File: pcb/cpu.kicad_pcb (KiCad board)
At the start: 2 copper layers, 270 parts, among them J1 Conn_01x05, J2 Conn_02x20_Odd_Even, J3 Conn_01x03, J4 Conn_02x20_Odd_Even, SW1 SW_DIP_x03 - Clock Source Sel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, SW2 SW_Push, SW4 SW_Push, U1 LM555, U10 74HCT574, U11 74LS283, U112 74LS574, U113 SST39SF040, U114 74HC04, U12 74HCT574, U121 74HCT574, U13 74LS273, U14 74LS283, U15 74LS273, U16 74HC245, U17 74HC238, U18 74HC245, U19 74HC238, U2 74HC14, U20 74HC238, U21 74HC00, U22 74LS283, U23 74LS283, U24 74HC245, U25 74HC245, U26 74HC00, U27 74LS283, U28 74LS283, U29 74HC245, U3 74151, U30 74HC86, U31 74HC245, U32 74HC00, U33 74LS08, U34 74LS283, U35 74LS107, U36 74HC238, U37 74LS138, U38 74LS574, U39 74HC590, U4 LM555 - Button Clock, U40 74LS283, U41 74HC245, U42 74HC245, U43 74HC00, U44 74HC00, U45 74HC00, U46 74HC00, U47 74HC00, U48 74HCT574, U49 74HCT574, U5 74HC04, U50 74HCT574, U51 74HCT574, U52 74HCT574, U53 74HCT574, U54 74HCT574, U55 74HCT574, U56 74HCT574, U57 74HCT574, U58 74HCT574, U59 74HCT574, U6 74HC590, U60 74HCT574, U61 74HCT574, U62 74HCT574, U63 74HCT574, U64 74HCT574, U65 74HCT574, U66 74LS32, U67 74HCT574, U68 74HCT574, U69 74HCT574, U7 74LS574, U70 74HCT574, U71 SST39SF040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

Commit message: About to try reducing by 1 EEPROM and reducing number of chips.
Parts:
- moved C103 394.5 mm to (211.5, 43.5)
- moved U86 394.5 mm to (215.0, 50.0)
- moved C17 331.6 mm to (155.5, 122.0)
- moved C18 331.6 mm to (159.0, 94.0)
- moved C19 331.6 mm to (159.0, 105.5)
- moved C23 331.6 mm to (155.5, 94.0)
- moved C26 331.6 mm to (171.0, 117.5)
- moved C34 331.6 mm to (171.0, 132.0)
- moved C60 331.6 mm to (133.5, 125.0)
- moved D1 331.6 mm to (167.0, 118.5)
- moved D2 331.6 mm to (167.0, 122.0)
- moved D3 331.6 mm to (167.0, 125.5)
- moved D4 331.6 mm to (167.0, 129.0)
- moved D5 331.6 mm to (167.0, 132.5)
- moved D6 331.6 mm to (167.0, 136.0)
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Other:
- board outline added: 235 x 190 mm
- net class CLK_NETS added: clearance 0.5, trace_width 0.2, via_dia 0.6, via_drill 0.3
- net class Default: clearance 0.14 -> 0.1; trace_width 0.2 -> 0.1
- net class POWER_NETS added: clearance 0.2, trace_width 0.3, via_dia 0.6, via_drill 0.3
- rule trace_clearance: 0.14 -> 0.1
- rule trace_min: 0.2 -> 0.1
- board text added: "Clk Sel Change Latch"
- board text added: "MemePU Ver.2.67 - MEME EDITION"
- board text removed: "Registers"

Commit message: Removed 1 EEPROM and some other chips by moving BUS_OUT signals to multi-plane.
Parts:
- removed C106, C107, C124, C125: 0.1uF, Capacitor_THT:C_Disc_D6.0mm_W2.5mm_P5.00mm
- removed U113: SST39SF040, Package_DIP:DIP-32_W15.24mm_Socket
- removed U114: 74HC04, Package_DIP:DIP-14_W7.62mm_Socket
- removed U95, U96: 74LS154, Package_DIP:DIP-24_W7.62mm_Socket
- added C104: 0.1uF, Capacitor_THT:C_Disc_D6.0mm_W2.5mm_P5.00mm, F.Cu at (104.5, 59.0)
- added U91: 74LS154, Package_DIP:DIP-24_W7.62mm_Socket, F.Cu at (101.0, 57.5)
- moved C103 199.3 mm to (13.0, 61.0)
- moved C94 199.3 mm to (13.0, 49.5)
- moved U85 199.3 mm to (16.5, 56.5)
- moved U86 199.3 mm to (16.5, 67.5)
- moved C22 101.1 mm to (216.5, 23.5), turned to 270 degrees
- moved U10 96.8 mm to (220.0, 30.0), turned to 90 degrees
- moved C21 83.5 mm to (186.5, 23.5), turned to 270 degrees
- moved U9 78.4 mm to (190.0, 30.5), turned to 90 degrees
- moved RN1 76.4 mm to (152.5, 37.0)
- moved C20 65.7 mm to (156.5, 23.0), turned to 270 degrees
- moved J4 60.5 mm to (191.0, 17.0)
- moved U8 60.0 mm to (160.0, 30.0), turned to 90 degrees
- moved J2 59.5 mm to (131.5, 17.0)
- moved U39 58.1 mm to (39.5, 12.5)
- moved U20 54.0 mm to (123.5, 12.5), turned to 270 degrees
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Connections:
- J2 pad 10: /BUS10 -> /BUS4
- J2 pad 12: /BUS11 -> /BUS5
- J2 pad 14: /BUS12 -> /BUS6
- J2 pad 16: /BUS13 -> /BUS7
- J2 pad 18: /BUS14 -> /BUS8
- J2 pad 2: /BUS6 -> /BUS0
- J2 pad 20: /BUS15 -> /BUS9
- J2 pad 22: /BUS16 -> /BUS10
- J2 pad 24: /BUS17 -> /BUS11
- J2 pad 26: /BUS18 -> /BUS12
- J2 pad 28: /BUS19 -> /BUS13
- J2 pad 29: /BUS0 -> /ADDR0
- J2 pad 30: /BUS20 -> /BUS14
- J2 pad 31: /BUS1 -> /ADDR1
- J2 pad 32: /BUS21 -> /BUS15
- J2 pad 33: /BUS2 -> /ADDR2
- J2 pad 34: /BUS22 -> /BUS16
- J2 pad 35: /BUS3 -> /ADDR3
- J2 pad 36: /BUS23 -> /BUS17
- J2 pad 37: /BUS4 -> /ADDR4
- J2 pad 38: /BUS24 -> /BUS18
- J2 pad 39: /BUS5 -> /ADDR5
- J2 pad 4: /BUS7 -> /BUS1
- J2 pad 40: /BUS25 -> /BUS19
- J2 pad 6: /BUS8 -> /BUS2
- J2 pad 8: /BUS9 -> /BUS3
- J4 pad 1: /BUS26 -> /ADDR6
- J4 pad 10: /ADDR18 -> /BUS24
- J4 pad 11: /BUS31 -> /ADDR11
- J4 pad 12: /ADDR19 -> /BUS25
- J4 pad 13: /ADDR0 -> /ADDR12
- J4 pad 14: /ADDR20 -> /BUS26
- J4 pad 15: /ADDR1 -> /ADDR13
- J4 pad 16: /ADDR21 -> /BUS27
- J4 pad 17: /ADDR2 -> /ADDR14
- J4 pad 18: /ADDR22 -> /BUS28
- J4 pad 19: /ADDR3 -> /ADDR15
- J4 pad 2: /ADDR14 -> /BUS20
- J4 pad 20: /ADDR23 -> /BUS29
- J4 pad 21: /ADDR4 -> /ADDR16
- J4 pad 22: (no net) -> /BUS30
- J4 pad 23: /ADDR5 -> /ADDR17
- J4 pad 24: (no net) -> /BUS31
- J4 pad 25: /ADDR6 -> /ADDR18
- J4 pad 27: /ADDR7 -> /ADDR19
- J4 pad 29: /ADDR8 -> /ADDR20
- J4 pad 3: /BUS27 -> /ADDR7
- J4 pad 31: /ADDR9 -> /ADDR21
- J4 pad 33: /ADDR10 -> /ADDR22
- J4 pad 35: /ADDR11 -> /ADDR23
- J4 pad 37: /ADDR12 -> (no net)
- J4 pad 39: /ADDR13 -> (no net)
- J4 pad 4: /ADDR15 -> /BUS21
- J4 pad 5: /BUS28 -> /ADDR8
- J4 pad 6: /ADDR16 -> /BUS22
- J4 pad 7: /BUS29 -> /ADDR9
- J4 pad 8: /ADDR17 -> /BUS23
- J4 pad 9: /BUS30 -> /ADDR10
- U112 pad 2: /Control Logic/CTRL16 -> /Control Logic/CTRL8
- U112 pad 3: /Control Logic/CTRL17 -> /Control Logic/CTRL9
- U112 pad 4: /Control Logic/CTRL18 -> /Control Logic/CTRL10
- U112 pad 5: /Control Logic/CTRL19 -> /Control Logic/CTRL11
- U112 pad 6: /Control Logic/CTRL20 -> /Control Logic/CTRL12
- U112 pad 7: /Control Logic/CTRL21 -> /Control Logic/CTRL13
- U112 pad 8: /Control Logic/CTRL22 -> /Control Logic/CTRL14
- U112 pad 9: /Control Logic/CTRL23 -> /Control Logic/CTRL15
- U2 pad 8: (no net) -> /ALU/ZERO_OUT
- U2 pad 9: GND -> Net-(D1-Pad1)
- U37 pad 10: (no net) -> /Control Logic/~BUS1_OUT_NCLK
- U37 pad 11: (no net) -> /Control Logic/~BUS0_OUT_NCLK
- U37 pad 7: (no net) -> /Control Logic/~BUS3_OUT_NCLK
- U37 pad 9: (no net) -> /Control Logic/~BUS2_OUT_NCLK
- U38 pad 2: /Control Logic/CTRL16 -> /Control Logic/CTRL8
- U38 pad 3: /Control Logic/CTRL17 -> /Control Logic/CTRL9
- U38 pad 4: /Control Logic/CTRL18 -> /Control Logic/CTRL10
- U38 pad 5: /Control Logic/CTRL19 -> /Control Logic/CTRL11
- U38 pad 6: /Control Logic/CTRL20 -> /Control Logic/CTRL12
- U38 pad 7: /Control Logic/CTRL21 -> /Control Logic/CTRL13
- U38 pad 8: /Control Logic/CTRL22 -> /Control Logic/CTRL14
- U38 pad 9: /Control Logic/CTRL23 -> /Control Logic/CTRL15
- U40 pad 9: (no net) -> /ALU/CARRY_OUT
- U5 pad 10: (no net) -> /Control Logic/IN decoder/~S4
- U5 pad 11: GND -> /Control Logic/CTRL_IN4
- U5 pad 8: (no net) -> /~MMU_IN_CLK
- U5 pad 9: Net-(D1-Pad1) -> /Control Logic/MMU_IN_CLK
- U7 pad 2: /Control Logic/CTRL16 -> /Control Logic/CTRL8
- U7 pad 3: /Control Logic/CTRL17 -> /Control Logic/CTRL9
- U7 pad 4: /Control Logic/CTRL18 -> /Control Logic/CTRL10
- U7 pad 5: /Control Logic/CTRL19 -> /Control Logic/CTRL11
- U7 pad 6: /Control Logic/CTRL20 -> /Control Logic/CTRL12
- U7 pad 7: /Control Logic/CTRL21 -> /Control Logic/CTRL13
- U7 pad 8: /Control Logic/CTRL22 -> /Control Logic/CTRL14
- U7 pad 9: /Control Logic/CTRL23 -> /Control Logic/CTRL15
- U84 pad 2: /Control Logic/CTRL16 -> /Control Logic/CTRL8
- U84 pad 3: /Control Logic/CTRL17 -> /Control Logic/CTRL9
- U84 pad 4: /Control Logic/CTRL18 -> /Control Logic/CTRL10
- U84 pad 5: /Control Logic/CTRL19 -> /Control Logic/CTRL11
- U84 pad 6: /Control Logic/CTRL20 -> /Control Logic/CTRL12
- U84 pad 7: /Control Logic/CTRL21 -> /Control Logic/CTRL13
- U84 pad 8: /Control Logic/CTRL22 -> /Control Logic/CTRL14
- U84 pad 9: /Control Logic/CTRL23 -> /Control Logic/CTRL15
- U89 pad 15: /Control Logic/CTRL_OUT4 -> (no net)
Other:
- board size 235 x 190 mm -> 235 x 178.5 mm
- board text added: "MemePU Ver.2.67"
- board text removed: "MemePU Ver.2.67 - MEME EDITION"

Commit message: Small changes.
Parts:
- added C105: 10nF, Capacitor_THT:C_Disc_D6.0mm_W2.5mm_P5.00mm, F.Cu at (125.5, 166.5)
- added D34: D, Diode_THT:D_DO-41_SOD81_P7.62mm_Horizontal, F.Cu at (129.1, 169.1)
- added R14: 100K, Resistor_THT:R_Axial_DIN0207_L6.3mm_D2.5mm_P7.62mm_Horizontal, F.Cu at (125.0, 172.5)
- added R17: 1M, Resistor_THT:R_Axial_DIN0207_L6.3mm_D2.5mm_P7.62mm_Horizontal, F.Cu at (132.5, 169.1)
- moved C118 20.0 mm to (17.5, 13.0), turned to 270 degrees
- moved C37 12.4 mm to (114.0, 172.5), turned to 0 degrees
- moved C82 10.5 mm to (153.0, 52.0)
- moved U75 10.5 mm to (149.5, 42.0)
- moved C15 9.01 mm to (95.0, 172.5), turned to 0 degrees
- moved U30 6.52 mm to (119.0, 161.5)
- moved SW1 5.90 mm to (103.5, 158.1)
- moved C5 5.52 mm to (84.5, 151.0)
- moved C6 5.52 mm to (84.5, 154.5)
- moved C7 5.52 mm to (84.5, 158.0)
- moved R4 5.52 mm to (120.5, 151.0)
- moved R5 5.52 mm to (120.5, 154.5)
- moved R6 5.52 mm to (92.0, 151.0)
- moved R7 5.52 mm to (92.0, 154.5)
- moved R8 5.52 mm to (92.0, 158.0)
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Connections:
- U33 pad 1: /Clock/PRE_CLK -> Net-(U33-Pad1)
- U33 pad 10: GND -> /Clock/PRE_CLK
- U33 pad 8: (no net) -> Net-(U33-Pad1)
- U33 pad 9: GND -> Net-(C105-Pad2)
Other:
- board size 235 x 178.5 mm -> 235 x 176.5 mm

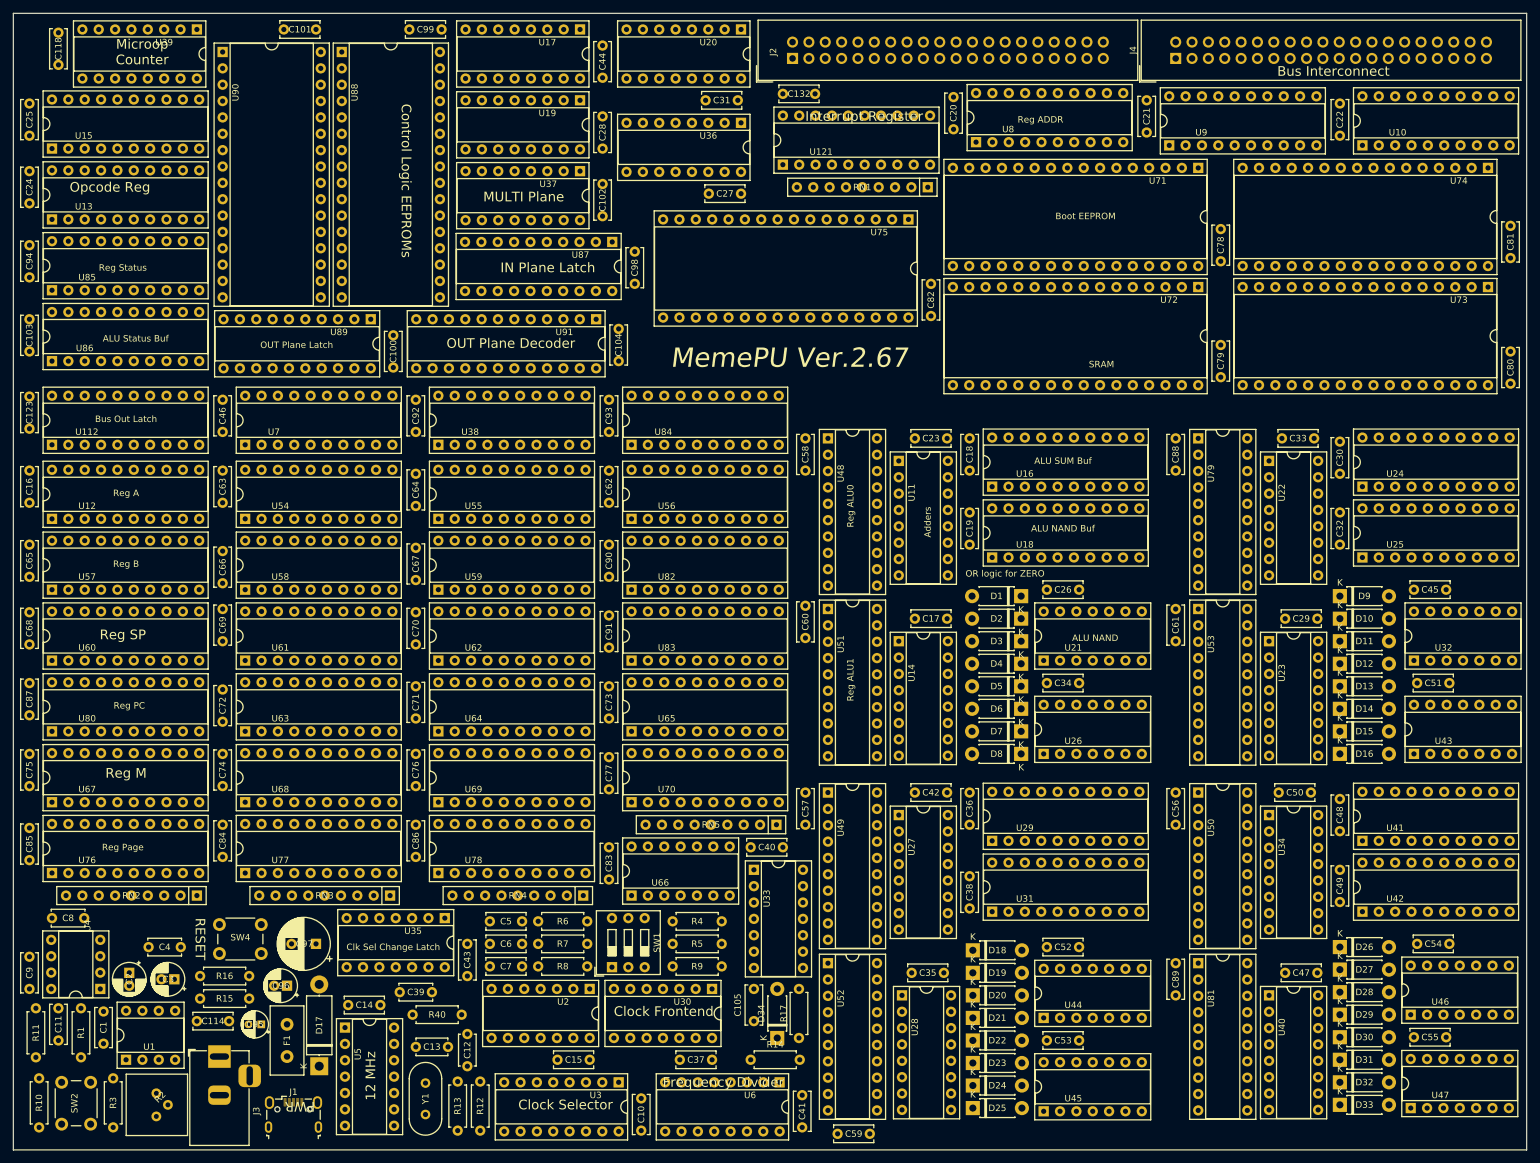
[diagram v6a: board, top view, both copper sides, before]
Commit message: Added traces for bypass caps and locked trackes.
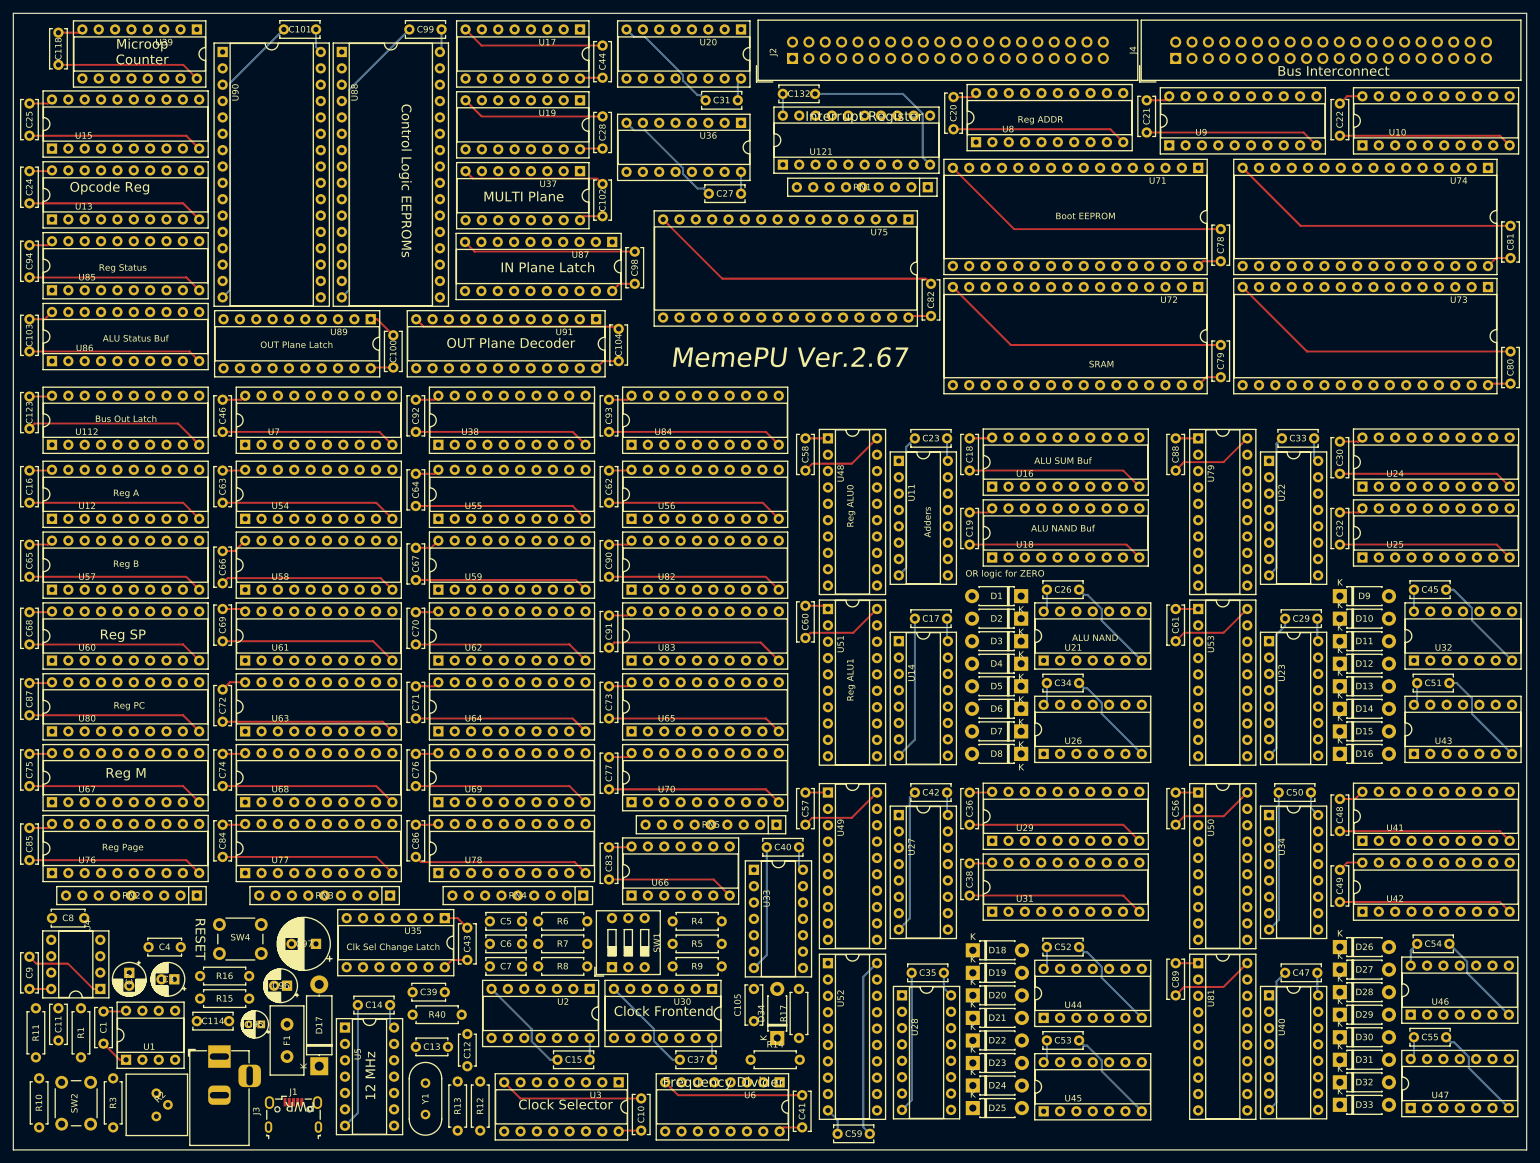
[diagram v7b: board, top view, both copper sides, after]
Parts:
- moved C38 7.00 mm to (159.0, 142.0), turned to 270 degrees
- moved C40 2.50 mm to (127.5, 139.5)
- moved C43 2.50 mm to (81.0, 152.0)
- moved C39 2.00 mm to (77.5, 162.0)
- moved C14 1.50 mm to (69.0, 164.0)
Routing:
- net GND: track 0.00 -> 2147.2 mm
- net VCC: track 0.00 -> 451.6 mm

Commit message: Add copy of pcb, pcb_smd. New smd project?
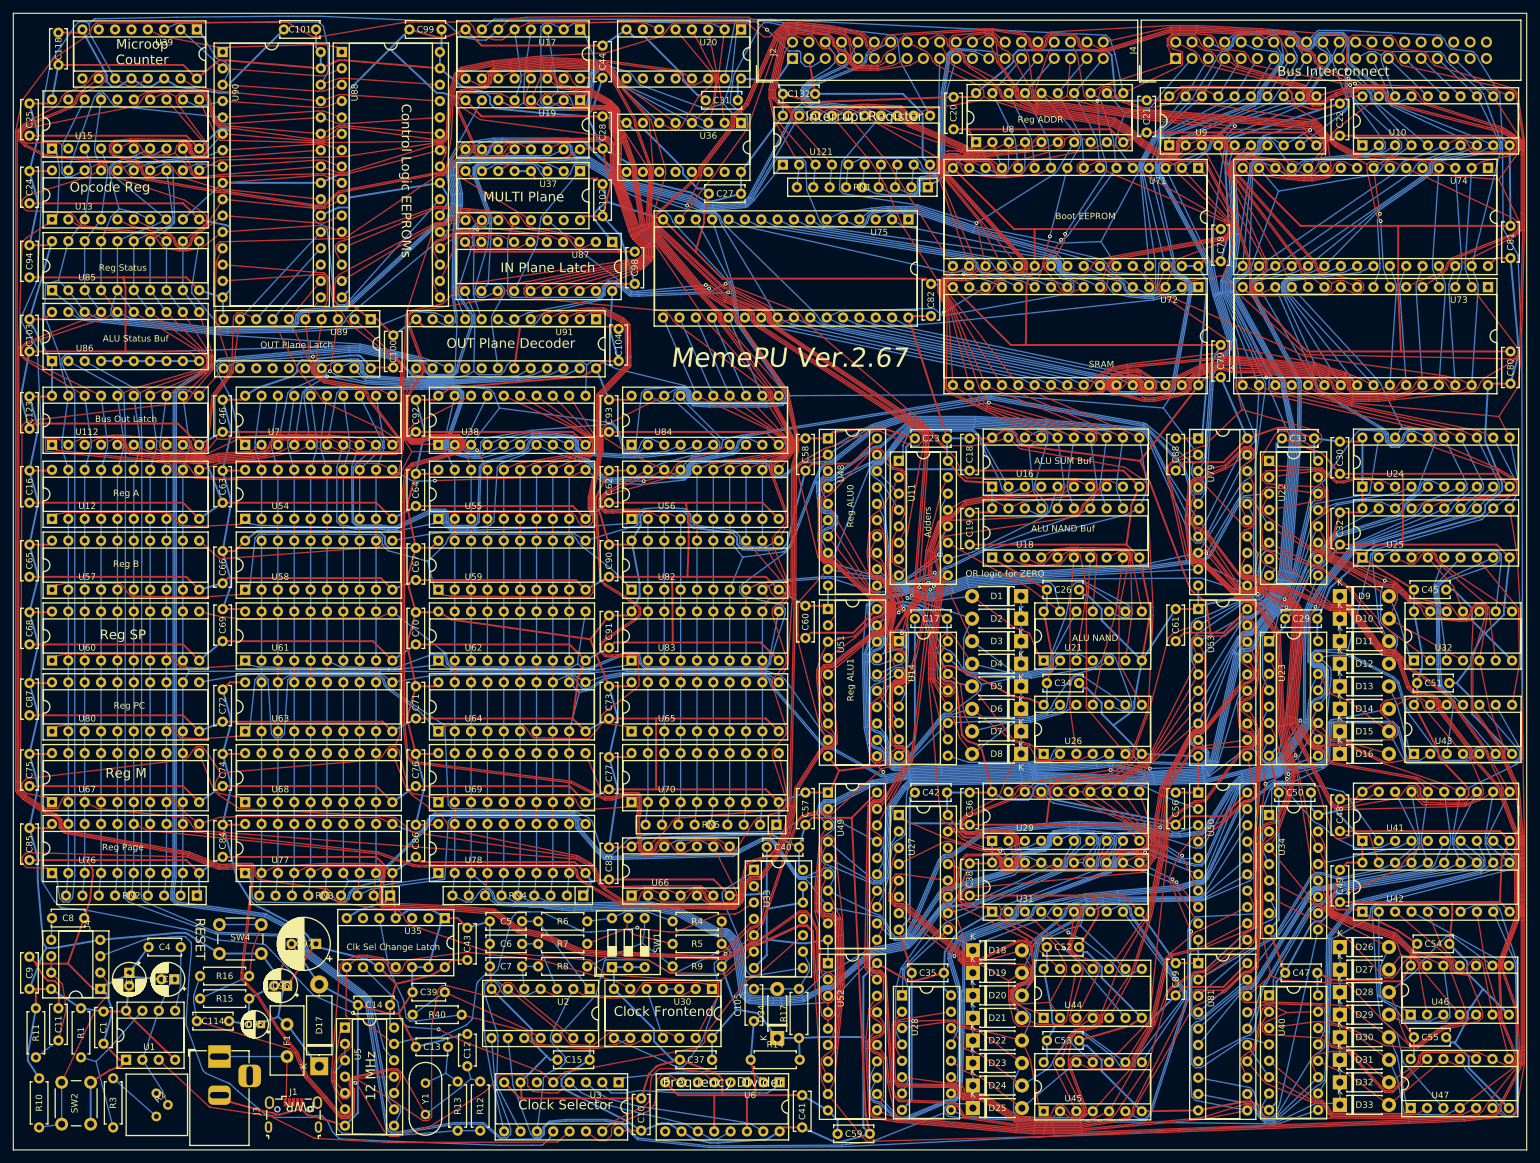
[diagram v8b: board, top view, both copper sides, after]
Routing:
- net VCC: track 451.6 -> 2144.3 mm
- net GND: track 2147.2 -> 3251.3 mm
- net /BUS15: track 0.00 -> 634.1 mm, vias 0 -> 1
- net /BUS6: track 0.00 -> 552.0 mm
- net /BUS12: track 0.00 -> 549.6 mm
- net /BUS2: track 0.00 -> 535.9 mm
- net /BUS5: track 0.00 -> 535.1 mm, vias 0 -> 1
- net /BUS1: track 0.00 -> 533.4 mm, vias 0 -> 1
- net /BUS4: track 0.00 -> 522.0 mm
- net /BUS3: track 0.00 -> 512.0 mm
- net /~MMU_IN_CLK: track 0.00 -> 510.1 mm, vias 0 -> 1
- net /BUS26: track 0.00 -> 504.2 mm
- net /BUS9: track 0.00 -> 504.2 mm
- net /BUS14: track 0.00 -> 502.2 mm, vias 0 -> 2
- net /BUS7: track 0.00 -> 501.9 mm
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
